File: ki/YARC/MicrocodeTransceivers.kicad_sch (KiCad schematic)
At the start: 0 parts

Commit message: Significant progress on microcode schematic. Minor improvements to MemorySystem.md.
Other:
- title: (none) -> Microcode Tranceivers
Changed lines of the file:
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@@
 (kicad_sch (version 20211123) (generator eeschema)
-  (paper "A4")
+  (paper "USLetter")
+  (title_block
+    (title "Microcode Tranceivers")
+    (date "2022-07-05")
+  )
 )

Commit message: Continue with microcode schematic
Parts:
- added U? (x2): 74LS574, symbol 74xx:74LS574
- added U? (x3): 74HC245, symbol 74xx:74HC245
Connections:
- new net GND: U?.1 (OE), U?.1 (OE), U?.10 (GND), U?.10 (GND), U?.10 (GND), U?.10 (GND), U?.10 (GND)
- new net IRCLK: U?.11 (Cp), U?.11 (Cp)
- new net IRH15: U?.12 (Q7), U?.2 (A0)
- new net IRH8: U?.19 (Q0), U?.9 (A7)
- new net IRL0: U?.19 (Q0), U?.9 (A7)
- new net IRL7: U?.12 (Q7), U?.2 (A0)
- new net KX0: U?.9 (A7)
- new net KX7: U?.2 (A0)
- new net READ/~{WRITE}: U?.1 (A->B)
- new net SYSDATA0: U?.11 (B7), U?.11 (B7), U?.2 (D0)
- new net SYSDATA15: U?.18 (B0), U?.9 (D7)
- new net SYSDATA7: U?.18 (B0), U?.18 (B0), U?.9 (D7)
- new net SYSDATA8: U?.11 (B7), U?.2 (D0)
- new net VCC: U?.1 (A->B), U?.1 (A->B), U?.20 (VCC), U?.20 (VCC), U?.20 (VCC), U?.20 (VCC), U?.20 (VCC)
- new net ~{IRHRD}: U?.19 (CE)
- new net ~{IRLRD}: U?.19 (CE)
- new net ~{WCS}: U?.19 (CE)
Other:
- note added: "INSTRUCTION REGISTER HIGH ALSO ON SHT 7"

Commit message: Continuing work on microcode control
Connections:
- net ~{IRLRD} is gone; now on net ~{IR_RD}: U?.19 (CE)
- net IRCLK renamed IR_CLK
- net ~{IRHRD} renamed ~{IR_RD}
- net ~{WCS} renamed ~{WCS_EN} (MCR0)
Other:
- note added: "INSTRUCTION REGISTER ALSO ON SHT 7"
- note removed: "INSTRUCTION REGISTER HIGH ALSO ON SHT 7"
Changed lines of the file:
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@@
     (stroke (width 0) (type default) (color 0 0 0 0))
   )
-  (text "INSTRUCTION REGISTER HIGH\nALSO ON SHT 7" (at 62.23 69.85 0)
+  (text "INSTRUCTION REGISTER\nALSO ON SHT 7" (at 68.58 71.12 0)
     (effects (font (size 1.27 1.27)) (justify left bottom))
   )
@@
     (effects (font (size 1.27 1.27)) (justify right bottom))
   )
-  (global_label "~{WCS}" (shape input) (at 64.77 134.62 0) (fields_autoplaced)
+  (global_label "~{WCS_EN} (MCR0)" (shape input) (at 64.77 134.62 0) (fields_autoplaced)
     (effects (font (size 1.27 1.27)) (justify left))
-    (property "Intersheet References" "${INTERSHEET_REFS}" (id 0) (at 71.1141 134.5406 0)
+    (property "Intersheet References" "${INTERSHEET_REFS}" (id 0) (at 82.4231 134.5406 0)
       (effects (font (size 1.27 1.27)) (justify left) hide)
     )
@@
     )
   )
-  (global_label "IRCLK" (shape input) (at 124.46 40.64 90) (fields_autoplaced)
+  (global_label "IR_CLK" (shape input) (at 124.46 40.64 90) (fields_autoplaced)
     (effects (font (size 1.27 1.27)) (justify left))
-    (property "Intersheet References" "${INTERSHEET_REFS}" (id 0) (at 124.3806 32.784 90)
+    (property "Intersheet References" "${INTERSHEET_REFS}" (id 0) (at 124.3806 31.8164 90)
       (effects (font (size 1.27 1.27)) (justify left) hide)
     )
   )
-  (global_label "IRCLK" (shape input) (at 63.5 40.64 90) (fields_autoplaced)
+  (global_label "IR_CLK" (shape input) (at 63.5 40.64 90) (fields_autoplaced)
     (effects (font (size 1.27 1.27)) (justify left))
-    (property "Intersheet References" "${INTERSHEET_REFS}" (id 0) (at 63.4206 32.784 90)
+    (property "Intersheet References" "${INTERSHEET_REFS}" (id 0) (at 63.4206 31.8164 90)
       (effects (font (size 1.27 1.27)) (justify left) hide)
     )
   )
-  (global_label "~{IRLRD}" (shape input) (at 241.3 66.04 270) (fields_autoplaced)
+  (global_label "~{IR_RD}" (shape input) (at 241.3 66.04 270) (fields_autoplaced)
     (effects (font (size 1.27 1.27)) (justify right))
-    (property "Intersheet References" "${INTERSHEET_REFS}" (id 0) (at 241.2206 73.896 90)
+    (property "Intersheet References" "${INTERSHEET_REFS}" (id 0) (at 241.2206 73.8355 90)
       (effects (font (size 1.27 1.27)) (justify right) hide)
     )
   )
-  (global_label "~{IRHRD}" (shape input) (at 186.69 66.04 270) (fields_autoplaced)
+  (global_label "~{IR_RD}" (shape input) (at 186.69 66.04 270) (fields_autoplaced)
     (effects (font (size 1.27 1.27)) (justify right))
-    (property "Intersheet References" "${INTERSHEET_REFS}" (id 0) (at 186.7694 74.1983 90)
+    (property "Intersheet References" "${INTERSHEET_REFS}" (id 0) (at 186.6106 73.8355 90)
       (effects (font (size 1.27 1.27)) (justify right) hide)
     )

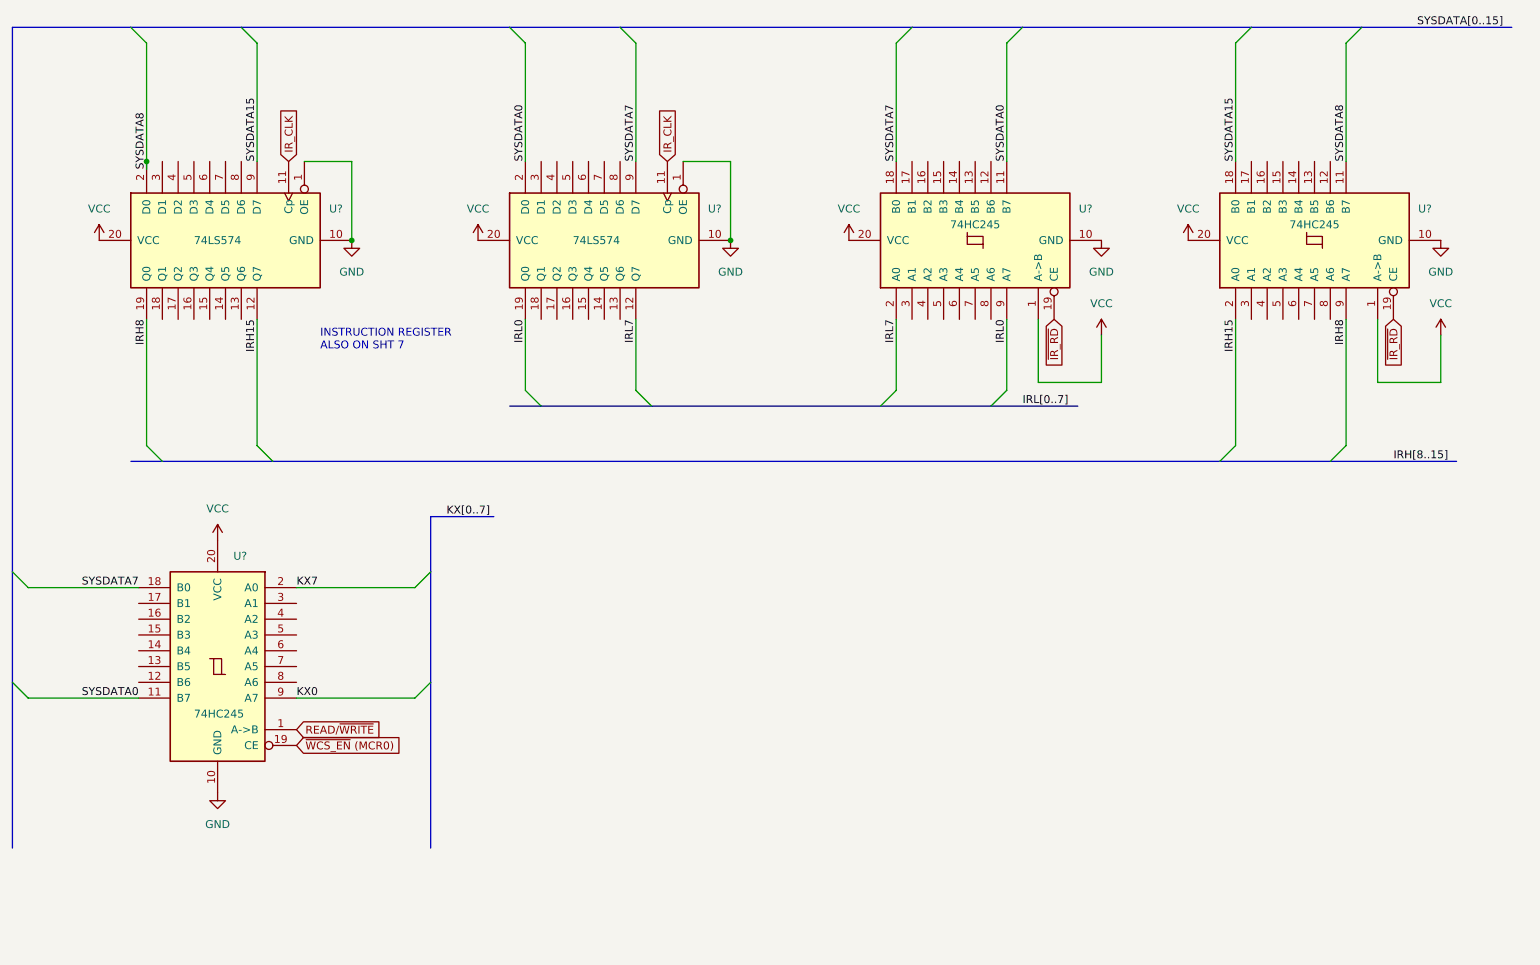
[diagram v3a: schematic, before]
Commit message: Assign part labels (U-numbers) in KiCad and start adding them to Fritzing layouts
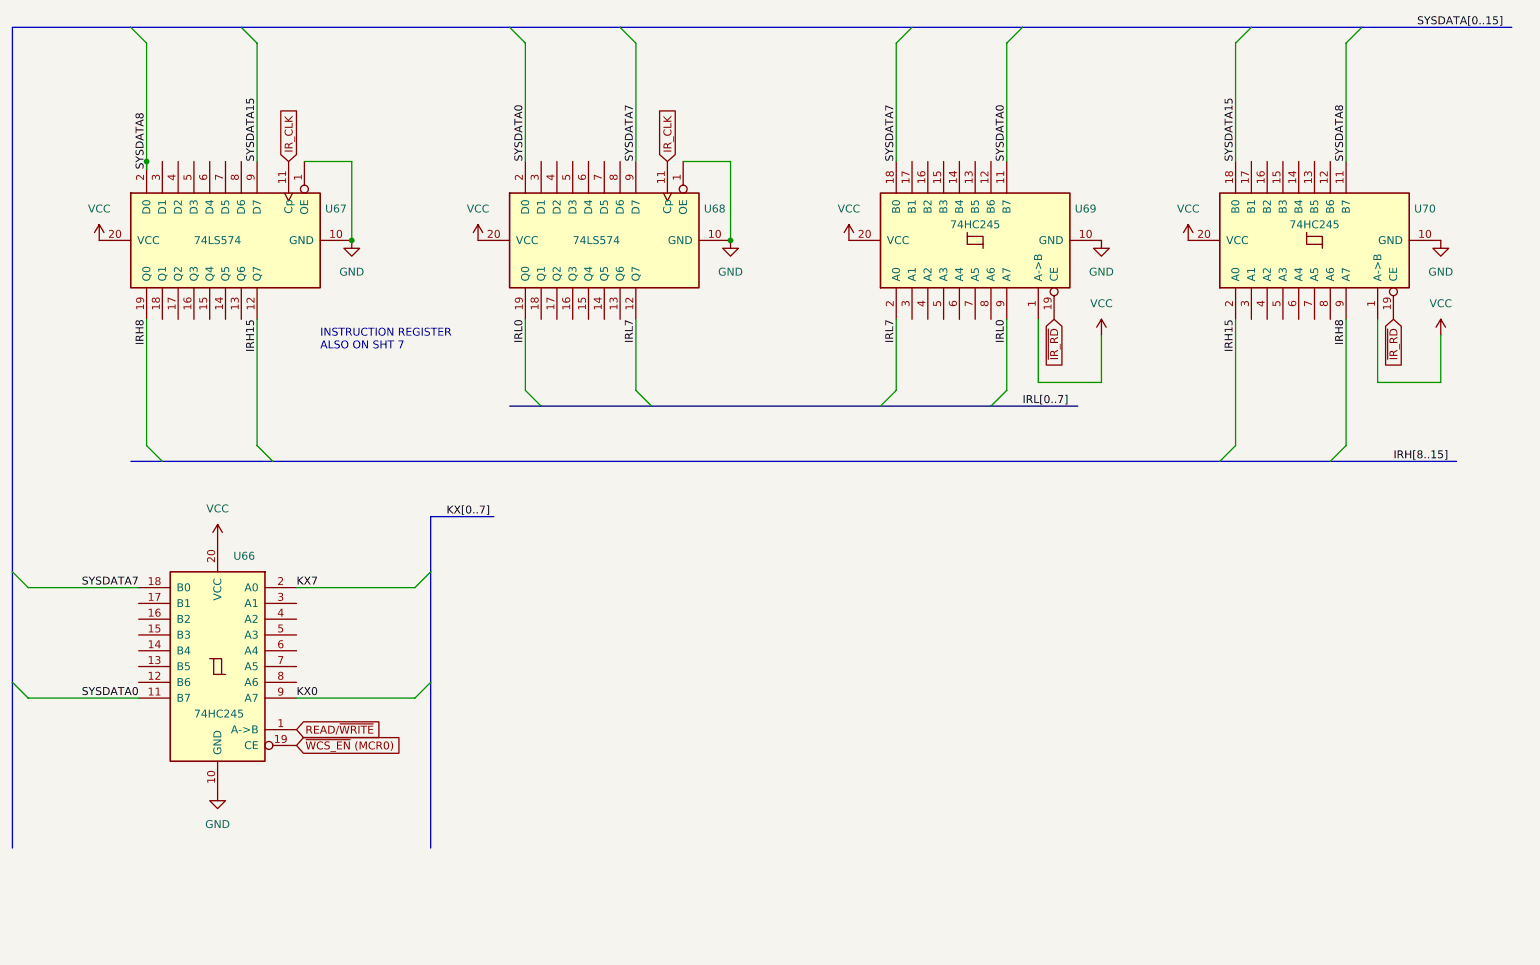
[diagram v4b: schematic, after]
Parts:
- gave numbers to parts that had none: 5
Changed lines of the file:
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@@
   (symbol (lib_id "74xx:74LS574") (at 114.3 53.34 90) (mirror x) (unit 1)
     (in_bom yes) (on_board yes)
-    (property "Reference" "U?" (id 0) (at 132.08 48.26 90))
+    (property "Reference" "U68" (id 0) (at 132.08 48.26 90))
     (property "Value" "74LS574" (id 1) (at 113.03 53.34 90))
     (property "Footprint" "" (id 2) (at 114.3 53.34 0)
@@
   (symbol (lib_id "power:VCC") (at 33.02 53.34 0) (unit 1)
     (in_bom yes) (on_board yes) (fields_autoplaced)
-    (property "Reference" "#PWR?" (id 0) (at 33.02 57.15 0)
+    (property "Reference" "#PWR0126" (id 0) (at 33.02 57.15 0)
       (effects (font (size 1.27 1.27)) hide)
     )
@@
   (symbol (lib_id "power:GND") (at 52.07 142.24 0) (unit 1)
     (in_bom yes) (on_board yes) (fields_autoplaced)
-    (property "Reference" "#PWR?" (id 0) (at 52.07 148.59 0)
+    (property "Reference" "#PWR0128" (id 0) (at 52.07 148.59 0)
       (effects (font (size 1.27 1.27)) hide)
     )
@@
   (symbol (lib_id "power:VCC") (at 194.31 68.58 0) (unit 1)
     (in_bom yes) (on_board yes)
-    (property "Reference" "#PWR?" (id 0) (at 194.31 72.39 0)
+    (property "Reference" "#PWR0134" (id 0) (at 194.31 72.39 0)
       (effects (font (size 1.27 1.27)) hide)
     )
@@
   (symbol (lib_id "74xx:74HC245") (at 173.99 53.34 90) (unit 1)
     (in_bom yes) (on_board yes)
-    (property "Reference" "U?" (id 0) (at 191.77 48.26 90))
+    (property "Reference" "U69" (id 0) (at 191.77 48.26 90))
     (property "Value" "74HC245" (id 1) (at 173.99 50.8 90))
     (property "Footprint" "" (id 2) (at 173.99 53.34 0)
@@
   (symbol (lib_id "74xx:74LS574") (at 53.34 53.34 90) (mirror x) (unit 1)
     (in_bom yes) (on_board yes)
-    (property "Reference" "U?" (id 0) (at 71.12 48.26 90))
+    (property "Reference" "U67" (id 0) (at 71.12 48.26 90))
     (property "Value" "74LS574" (id 1) (at 52.07 53.34 90))
     (property "Footprint" "" (id 2) (at 53.34 53.34 0)
@@
   (symbol (lib_id "74xx:74HC245") (at 52.07 121.92 0) (mirror y) (unit 1)
     (in_bom yes) (on_board yes)
-    (property "Reference" "U?" (id 0) (at 54.61 104.14 0)
+    (property "Reference" "U66" (id 0) (at 54.61 104.14 0)
       (effects (font (size 1.27 1.27)) (justify right))
     )
@@
   (symbol (lib_id "74xx:74HC245") (at 228.6 53.34 90) (unit 1)
     (in_bom yes) (on_board yes)
-    (property "Reference" "U?" (id 0) (at 246.38 48.26 90))
+    (property "Reference" "U70" (id 0) (at 246.38 48.26 90))
     (property "Value" "74HC245" (id 1) (at 228.6 50.8 90))
     (property "Footprint" "" (id 2) (at 228.6 53.34 0)
@@
   (symbol (lib_id "power:VCC") (at 208.28 53.34 0) (unit 1)
     (in_bom yes) (on_board yes) (fields_autoplaced)
-    (property "Reference" "#PWR?" (id 0) (at 208.28 57.15 0)
+    (property "Reference" "#PWR0135" (id 0) (at 208.28 57.15 0)
       (effects (font (size 1.27 1.27)) hide)
     )
@@
   (symbol (lib_id "power:GND") (at 248.92 53.34 0) (unit 1)
     (in_bom yes) (on_board yes) (fields_autoplaced)
-    (property "Reference" "#PWR?" (id 0) (at 248.92 59.69 0)
+    (property "Reference" "#PWR0136" (id 0) (at 248.92 59.69 0)
       (effects (font (size 1.27 1.27)) hide)
     )
@@
   (symbol (lib_id "power:VCC") (at 248.92 68.58 0) (unit 1)
     (in_bom yes) (on_board yes)
-    (property "Reference" "#PWR?" (id 0) (at 248.92 72.39 0)
+    (property "Reference" "#PWR0137" (id 0) (at 248.92 72.39 0)
       (effects (font (size 1.27 1.27)) hide)
     )
@@
   (symbol (lib_id "power:VCC") (at 93.98 53.34 0) (unit 1)
     (in_bom yes) (on_board yes)
-    (property "Reference" "#PWR?" (id 0) (at 93.98 57.15 0)
+    (property "Reference" "#PWR0130" (id 0) (at 93.98 57.15 0)
       (effects (font (size 1.27 1.27)) hide)
     )
@@
   (symbol (lib_id "power:VCC") (at 153.67 53.34 0) (unit 1)
     (in_bom yes) (on_board yes) (fields_autoplaced)
-    (property "Reference" "#PWR?" (id 0) (at 153.67 57.15 0)
+    (property "Reference" "#PWR0132" (id 0) (at 153.67 57.15 0)
       (effects (font (size 1.27 1.27)) hide)
     )
@@
   (symbol (lib_id "power:VCC") (at 52.07 101.6 0) (unit 1)
     (in_bom yes) (on_board yes) (fields_autoplaced)
-    (property "Reference" "#PWR?" (id 0) (at 52.07 105.41 0)
+    (property "Reference" "#PWR0127" (id 0) (at 52.07 105.41 0)
       (effects (font (size 1.27 1.27)) hide)
     )
@@
   (symbol (lib_id "power:GND") (at 194.31 53.34 0) (unit 1)
     (in_bom yes) (on_board yes) (fields_autoplaced)
-    (property "Reference" "#PWR?" (id 0) (at 194.31 59.69 0)
+    (property "Reference" "#PWR0133" (id 0) (at 194.31 59.69 0)
       (effects (font (size 1.27 1.27)) hide)
     )
@@
   (symbol (lib_id "power:GND") (at 73.66 53.34 0) (unit 1)
     (in_bom yes) (on_board yes) (fields_autoplaced)
-    (property "Reference" "#PWR?" (id 0) (at 73.66 59.69 0)
+    (property "Reference" "#PWR0129" (id 0) (at 73.66 59.69 0)
       (effects (font (size 1.27 1.27)) hide)
     )
@@
   (symbol (lib_id "power:GND") (at 134.62 53.34 0) (unit 1)
     (in_bom yes) (on_board yes) (fields_autoplaced)
-    (property "Reference" "#PWR?" (id 0) (at 134.62 59.69 0)
-      (effects (font (size 1.27 1.27)) hide)
-    )
+    (property "Reference" "#PWR0131" (id 0) (at 134.62 59.69 0)
+      (effects (font (size 1.27 1.27)) hide)
+    )

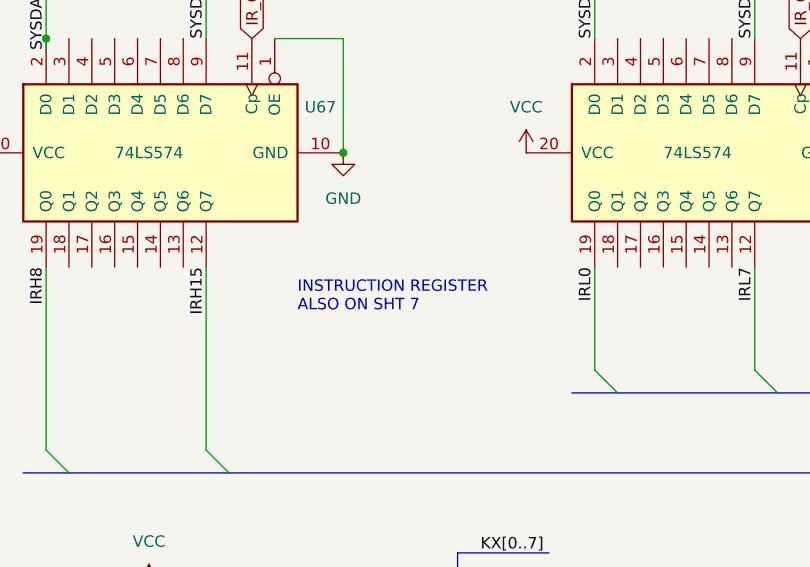
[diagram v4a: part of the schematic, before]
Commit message: Continue annotating and labeling ICs
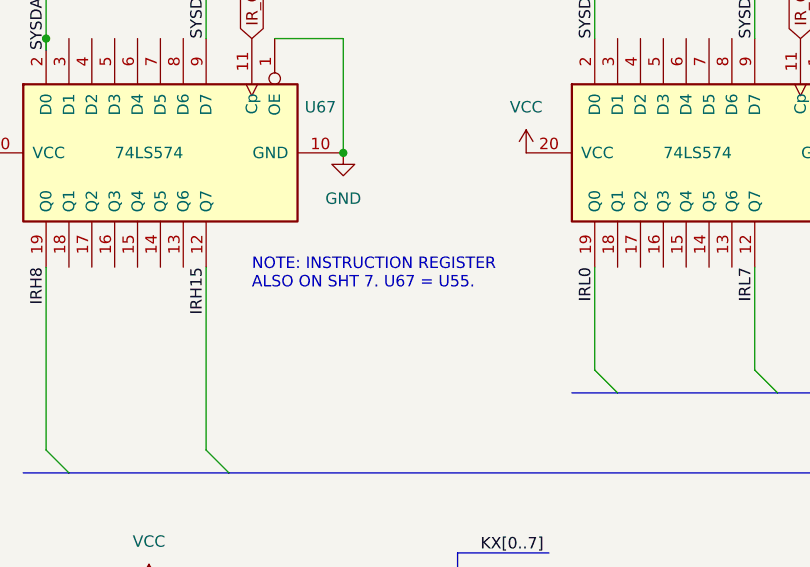
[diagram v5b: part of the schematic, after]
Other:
- note added: "NOTE: INSTRUCTION REGISTER ALSO ON SHT 7. U67 = U55."
- note removed: "INSTRUCTION REGISTER ALSO ON SHT 7"
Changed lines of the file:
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@@
     (stroke (width 0) (type default) (color 0 0 0 0))
   )
-  (text "INSTRUCTION REGISTER\nALSO ON SHT 7" (at 68.58 71.12 0)
+  (text "NOTE: INSTRUCTION REGISTER\nALSO ON SHT 7. U67 = U55."
+    (at 63.5 68.58 0)
     (effects (font (size 1.27 1.27)) (justify left bottom))
   )
